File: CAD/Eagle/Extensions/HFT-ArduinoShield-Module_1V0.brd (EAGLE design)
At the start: 80 x 96.5 mm, 14 parts, among them X201 2X20/90_1MM27_HARWIN_M50-3902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, X202 2X20/90_1MM27_HARWIN_M50-3902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

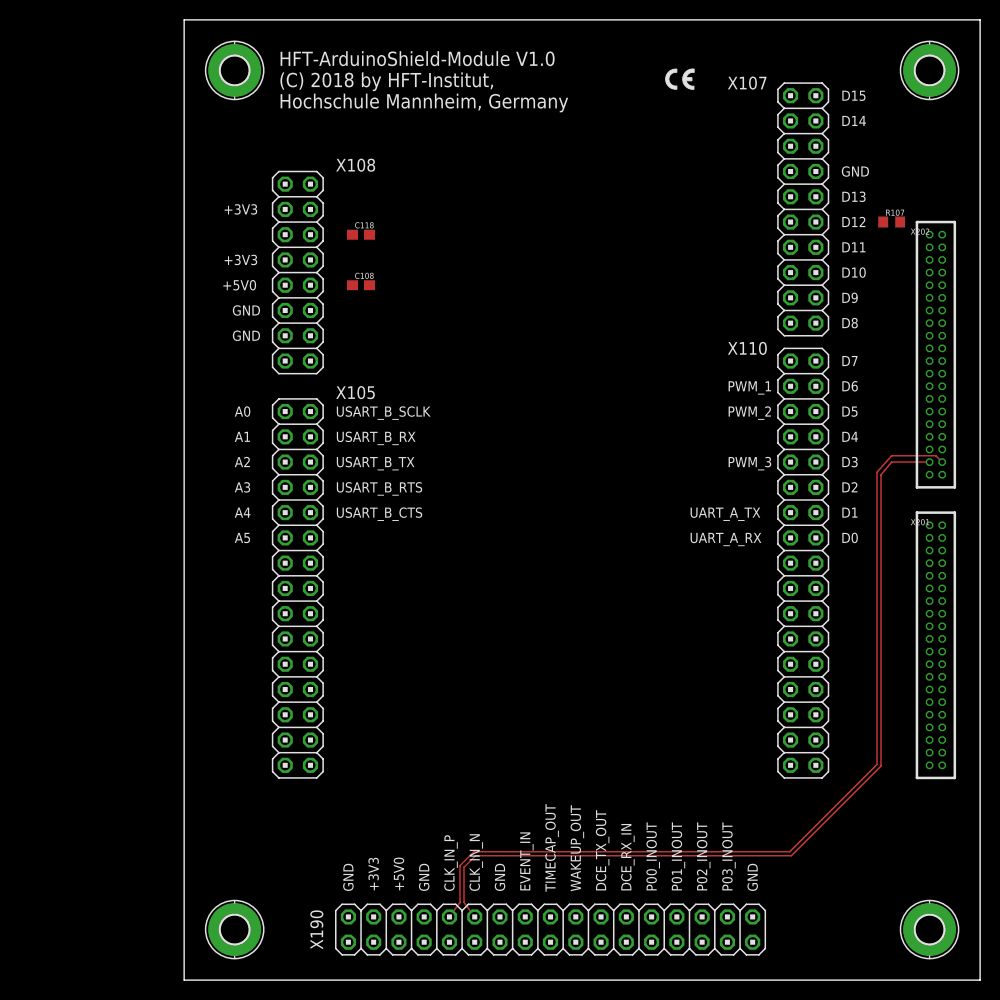
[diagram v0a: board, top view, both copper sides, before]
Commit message: HW_ARDUINO - first try of layout
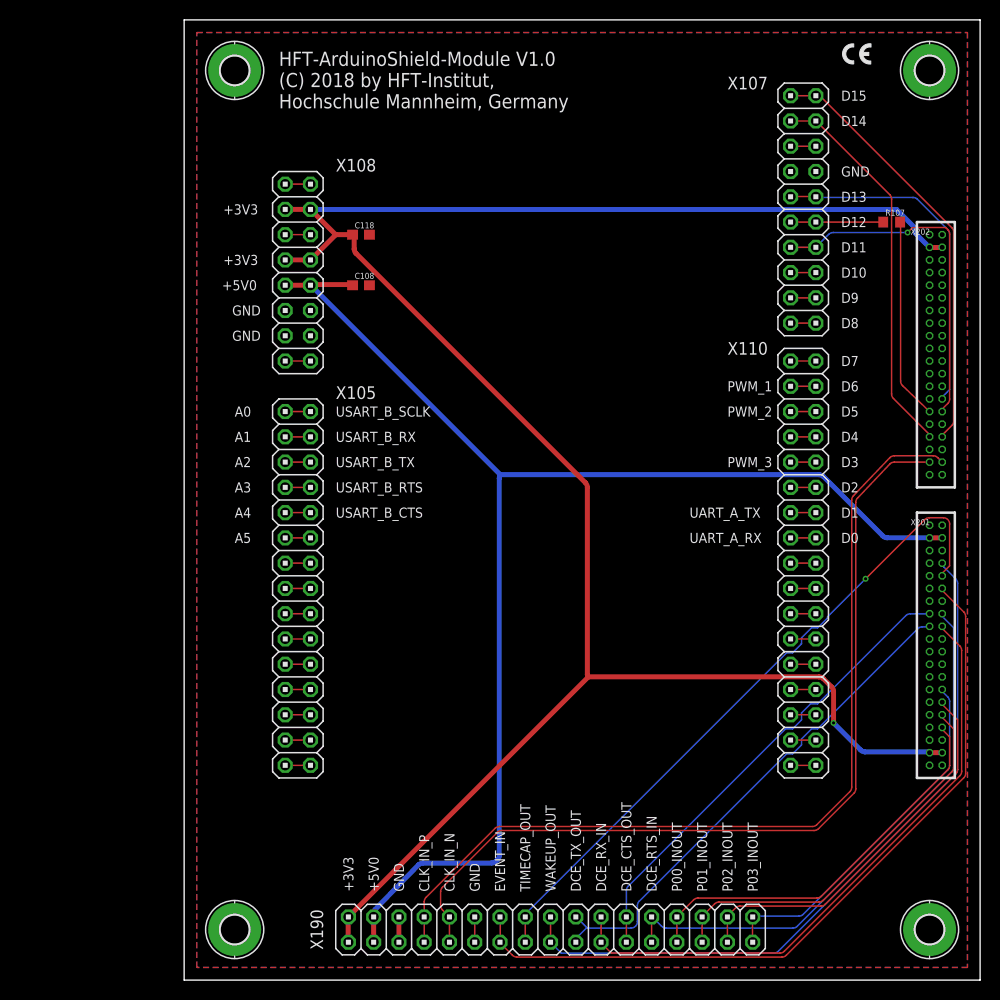
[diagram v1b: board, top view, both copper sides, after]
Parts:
- C108, C118: value (none) -> 100nF
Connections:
- net +3V3: now also X190.1, X190.2; no longer X190.3, X190.4
- net +5V0: now also X190.3, X190.4; no longer X190.5, X190.6
- net CLK_IN_N: now also X190.10, X190.9; no longer X190.11, X190.12
- net CLK_IN_P: now also X190.7, X190.8; no longer X190.10, X190.9
- net DCE_CTS_OUT: now also X190.23, X190.24
- net DCE_RTS_IN: now also X190.25, X190.26
- net DCE_RX_IN: now also X190.21, X190.22; no longer X190.23, X190.24
- net DCE_TX_OUT: now also X190.19, X190.20; no longer X190.21, X190.22
- net EVENT_IN: now also X190.13, X190.14; no longer X190.15, X190.16
- net GND: now also X190.11, X190.12, X190.5, X190.6; no longer X190.1, X190.13, X190.14, X190.2, X190.33, X190.34, X190.7, X190.8
- net P00: now also X190.27, X190.28; no longer X190.25, X190.26
- net P01: now also X190.29, X190.30; no longer X190.27, X190.28
- net P02: now also X190.31, X190.32; no longer X190.29, X190.30
- net P03: now also X190.33, X190.34; no longer X190.31, X190.32
- net TIMCAP_OUT: now also X190.15, X190.16; no longer X190.17, X190.18
- net WAKEUP_OUT: now also X190.17, X190.18; no longer X190.19, X190.20
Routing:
- net +3V3: track 0.00 -> 210.8 mm, vias 0 -> 1
- net +5V0: track 0.00 -> 137.2 mm
- net EVENT_IN: track 0.00 -> 77.2 mm
- net WAKEUP_OUT: track 0.00 -> 72.9 mm
- net TIMCAP_OUT: track 0.00 -> 68.1 mm, vias 0 -> 1
- net DCE_RX_IN: track 0.00 -> 62.2 mm
- net DCE_RTS_IN: track 0.00 -> 56.0 mm
- net DCE_TX_OUT: track 0.00 -> 51.9 mm
- net DCE_CTS_OUT: track 0.00 -> 47.7 mm
- net I2C_SCL_IN: track 0.00 -> 43.2 mm
- net P00: track 0.00 -> 40.4 mm
- net P01: track 0.00 -> 39.9 mm
- net P02: track 0.00 -> 39.3 mm
- net I2C_SDA_INOUT: track 0.00 -> 39.0 mm
- net P03: track 0.00 -> 36.6 mm
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- added copper zone on layer 1, net GND
- added copper zone on layer 16, net GND
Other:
- board text added: "DCE_CTS_OUT"
- board text added: "DCE_RTS_IN"

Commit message: HW_ARDUINO - Raspberry Pi socket added, also
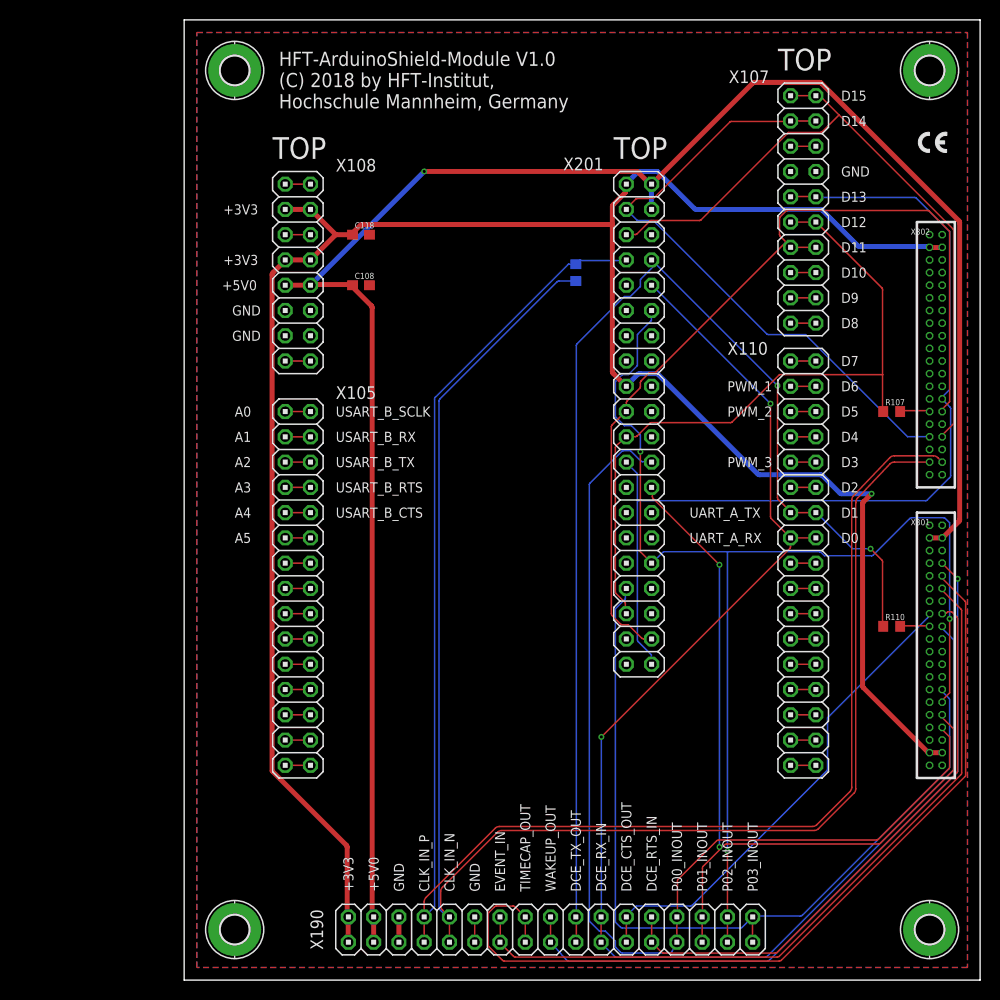
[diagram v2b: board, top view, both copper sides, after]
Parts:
- added R110: 47R, df4iah_rcl:R0603
- added R201: 120R, df4iah_rcl:R0603
- added X301: 2X20/90_1MM27_HARWIN_M50-3902042_HEADER, df4iah_connector:2X20/90_1MM27_HARWIN_M50-3902042_HEADER
- X201: value 2X20/90_1MM27_HARWIN_M50-3902042_HEADER -> (none); device df4iah_connector:2X20/90_1MM27_HARWIN_M50-3902042_HEADER -> df4iah_connector:2X20
- moved X201 38.9 mm to (62.2, 57.1), turned to 270 degrees
- moved R107 19.1 mm to (87.6, 57.1)
- renumbered H301 to H401, H302 to H402, H303 to H403, H304 to H404, X202 to X302
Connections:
- removed net N107_11: R107.1, X107.11, X107.12
- removed net N110_13: X110.13, X110.14
- removed net N110_15: X110.15, X110.16
- new net DCE_TX_OUT_R: R110.1, X110.13, X110.14, X190.19, X190.20, X201.8
- new net SPI_MISO_OUT_R: R107.1, X107.11, X107.12, X201.21, X201.35
- net +3V3: now also X201.1, X201.17, X301.3, X301.4; no longer X201.3, X201.4
- net +5V0: now also X201.2, X201.4, X301.37, X301.38; no longer X201.37, X201.38
- net CLK_IN_N: now also R201.1
- net CLK_IN_P: now also R201.2, X201.7
- net DCE_CTS_OUT: now also X301.26; no longer X201.26
- net DCE_RTS_IN: now also X301.25; no longer X201.25
- net DCE_RX_IN: now also X110.15, X110.16, X201.10, X301.23; no longer X201.23
- net DCE_TX_OUT: now also R110.2, X301.24; no longer X190.19, X190.20, X201.24
- net EVENT_IN: now also X301.29; no longer X201.29
- net GND: now also X201.20, X201.25, X201.9, X301.1, X301.10, X301.12, X301.14, X301.2, X301.21, X301.22, X301.27, X301.28, X301.30, X301.32, X301.34, X301.35, X301.36, X301.39, X301.40, X301.5, X301.6, X301.8; no longer X201.1, X201.10, X201.12, X201.2, X201.21, X201.22, X201.27, X201.28, X201.32, X201.35, X201.36, X201.40, X201.5, X201.8
- net I2C_SCL_IN: now also X201.5
- net I2C_SDA_INOUT: now also X201.3
- net P00: now also X201.24, X301.7; no longer X201.7
- net P01: now also X201.26, X301.9; no longer X201.9
- net P02: now also X201.12, X201.32, X301.11; no longer X201.11
- net P03: now also X201.33, X301.13; no longer X201.13
- net SPI_MOSI_IN: now also X201.19, X201.38
- net SPI_SCK_IN: now also X201.23, X201.40
- net TIMCAP_OUT: now also X301.31; no longer X201.31
- net WAKEUP_OUT: now also X301.33; no longer X201.33
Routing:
- net DCE_TX_OUT_R: track 0.00 -> 121.5 mm, vias 0 -> 2
- net P02: track 39.3 -> 119.1 mm, vias 0 -> 3
- net DCE_RX_IN: track 62.2 -> 141.0 mm, vias 0 -> 2
- net CLK_IN_P: track 92.1 -> 169.7 mm
- net SPI_MISO_OUT_R: track 0.00 -> 71.4 mm
- net CLK_IN_N: track 89.6 -> 160.9 mm
- net P00: track 40.4 -> 105.7 mm
- net SPI_SCK_IN: track 34.5 -> 96.5 mm
- net SPI_MOSI_IN: track 35.3 -> 93.3 mm, vias 1 -> 0
- net +5V0: track 137.2 -> 190.5 mm, vias 0 -> 1
- net DCE_TX_OUT: track 51.9 -> 3.00 mm
- net P03: track 36.6 -> 85.2 mm
- net P01: track 39.9 -> 82.0 mm, vias 0 -> 2
- net I2C_SCL_IN: track 43.2 -> 69.6 mm
- net I2C_SDA_INOUT: track 39.0 -> 62.7 mm
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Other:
- board text added: "TOP"

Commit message: HW_ARDUINO - Interconnect between PI socket and Arduino sockets added
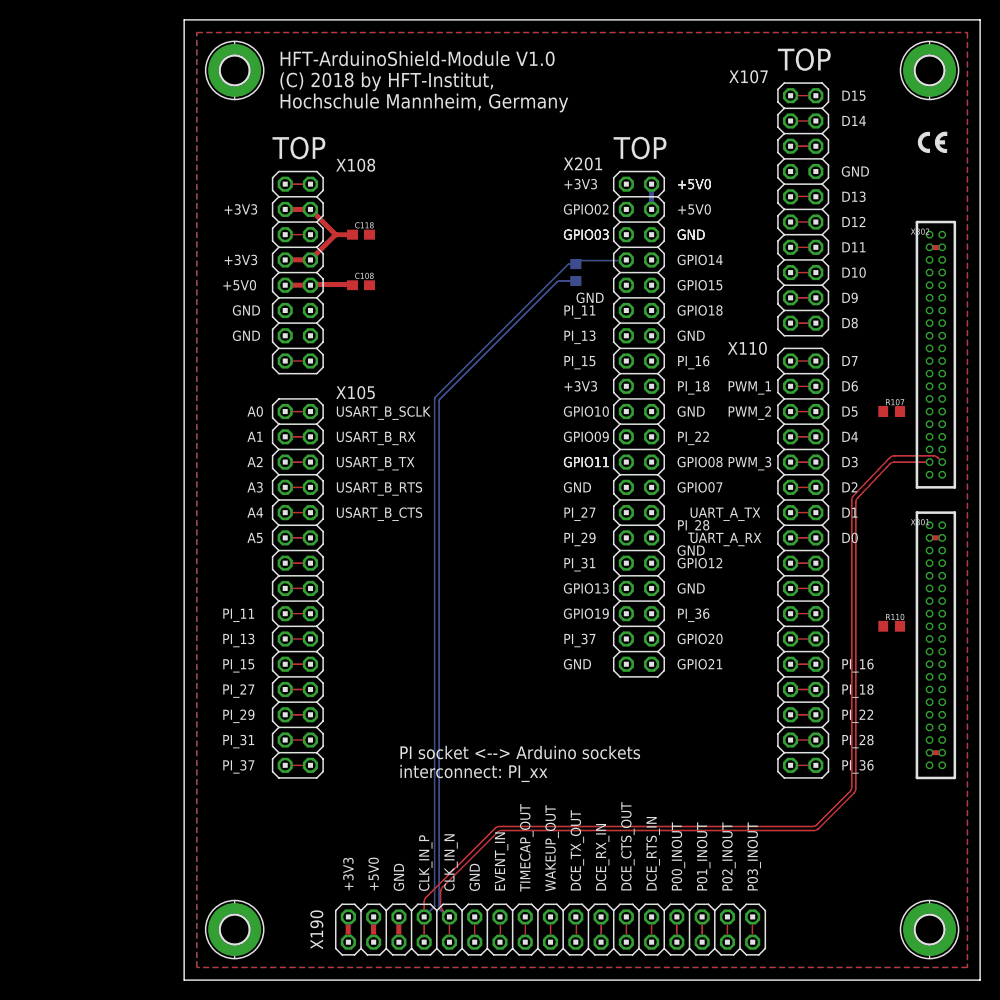
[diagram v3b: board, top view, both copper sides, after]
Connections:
- removed net N105_17: X105.17, X105.18
- removed net N105_19: X105.19, X105.20
- removed net N105_21: X105.21, X105.22
- removed net N105_23: X105.23, X105.24
- removed net N105_25: X105.25, X105.26
- removed net N105_27: X105.27, X105.28
- removed net N105_29: X105.29, X105.30
- removed net N110_25: X110.25, X110.26
- removed net N110_27: X110.27, X110.28
- removed net N110_29: X110.29, X110.30
- removed net N110_31: X110.31, X110.32
- removed net N110_33: X110.33, X110.34
- new net PI_11: X105.17, X105.18, X201.11
- new net PI_13: X105.19, X105.20, X201.13
- new net PI_15: X105.21, X105.22, X201.15
- new net PI_16: X110.25, X110.26, X201.16
- new net PI_18: X110.27, X110.28, X201.18
- new net PI_22: X110.29, X110.30, X201.22
- new net PI_27: X105.23, X105.24, X201.27
- new net PI_28: X110.31, X110.32, X201.28
- new net PI_29: X105.25, X105.26, X201.29
- new net PI_31: X105.27, X105.28, X201.31
- new net PI_36: X110.33, X110.34, X201.36
- new net PI_37: X105.29, X105.30, X201.37
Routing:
- net +3V3: track 230.4 -> 19.1 mm, vias 1 -> 0
- net +5V0: track 190.5 -> 13.2 mm, vias 1 -> 0
- net DCE_RX_IN: track 141.0 -> 5.08 mm, vias 2 -> 0
- net P02: track 119.1 -> 2.54 mm, vias 3 -> 0
- net DCE_TX_OUT_R: track 121.5 -> 5.17 mm, vias 2 -> 0
- net P00: track 105.7 -> 2.54 mm
- net SPI_SCK_IN: track 96.5 -> 2.56 mm
- net SPI_MOSI_IN: track 93.3 -> 2.54 mm
- net TIMCAP_OUT: track 87.6 -> 2.54 mm
- net P03: track 85.2 -> 2.56 mm
- net P01: track 82.0 -> 2.54 mm, vias 2 -> 0
- net EVENT_IN: track 76.6 -> 2.58 mm
- net WAKEUP_OUT: track 73.8 -> 2.54 mm, vias 1 -> 0
- net SPI_MISO_OUT_R: track 71.4 -> 2.54 mm
- net I2C_SCL_IN: track 69.6 -> 2.54 mm
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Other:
- board text added: "GPIO02"
- board text added: "GPIO03"
- board text added: "GPIO07"
- board text added: "GPIO08"
- board text added: "GPIO09"
- board text added: "GPIO10"
- board text added: "GPIO11"
- board text added: "GPIO12"
- board text added: "GPIO13"
- board text added: "GPIO14"
- board text added: "GPIO15"
- board text added: "GPIO18"
- board text added: "GPIO19"
- board text added: "GPIO20"
- board text added: "GPIO21"
- board text added: "PI socket <--> Arduino sockets interconnect: PI_xx"
- board text added: "PI_11"
- board text added: "PI_13"
- board text added: "PI_15"
- board text added: "PI_16"
- board text added: "PI_18"
- board text added: "PI_22"
- board text added: "PI_27"
- board text added: "PI_28"
- board text added: "PI_29"
- board text added: "PI_31"
- board text added: "PI_36"
- board text added: "PI_37"

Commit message: HW_ARDUINO - placing and routing done
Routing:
- net +3V3: track 19.1 -> 227.7 mm, vias 0 -> 2
- net +5V0: track 13.2 -> 190.2 mm
- net P02: track 2.54 -> 155.2 mm, vias 0 -> 3
- net DCE_RX_IN: track 5.08 -> 135.8 mm, vias 0 -> 4
- net DCE_TX_OUT_R: track 5.17 -> 126.8 mm, vias 0 -> 2
- net P00: track 2.54 -> 103.3 mm, vias 0 -> 1
- net SPI_SCK_IN: track 2.56 -> 97.6 mm
- net SPI_MOSI_IN: track 2.54 -> 89.1 mm, vias 0 -> 3
- net P01: track 2.54 -> 87.9 mm, vias 0 -> 1
- net P03: track 2.56 -> 86.7 mm
- net TIMCAP_OUT: track 2.54 -> 85.1 mm
- net EVENT_IN: track 2.58 -> 76.6 mm
- net SPI_MISO_OUT_R: track 2.54 -> 76.2 mm
- net WAKEUP_OUT: track 2.54 -> 73.6 mm
- net I2C_SCL_IN: track 2.54 -> 65.5 mm
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
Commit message: HW_ARDUINO - last positioning and small fixes
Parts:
- moved R201 16.5 mm to (39.4, 71.1)
- moved X105 16.5 mm to (11.4, 38.1)
- moved X108 16.5 mm to (11.4, 71.1)
- moved C108 16.5 mm to (17.8, 69.8)
- moved C118 16.5 mm to (17.8, 74.9)
- moved H402 16.5 mm to (5.08, 91.4)
- moved H403 16.5 mm to (5.08, 5.08)
- moved X107 16.5 mm to (62.2, 77.5)
- moved X110 16.5 mm to (62.2, 40.6)
- moved X190 16.5 mm to (38.1, 5.08)
- moved X201 16.5 mm to (45.7, 57.1)
- moved H401 16.5 mm to (74.9, 91.4)
- moved H404 16.5 mm to (74.9, 5.08)
- moved R107 16.5 mm to (71.1, 57.1)
- moved R110 16.5 mm to (71.1, 35.6)
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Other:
- board text added: "TOP of Ard."
- board text added: "TOP of Pi"
- board text removed: "TOP"
